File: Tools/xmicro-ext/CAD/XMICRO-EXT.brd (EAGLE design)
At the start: 101.6 x 101.6 mm, 2 parts

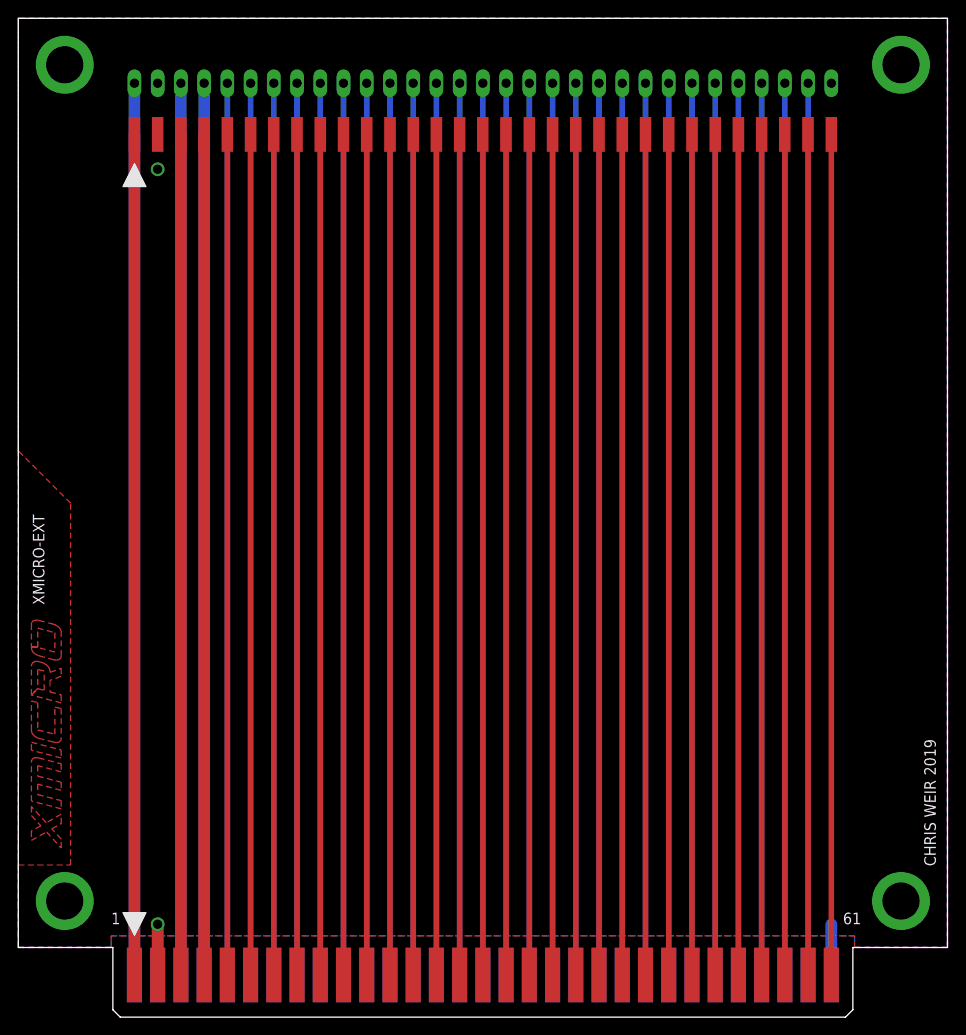
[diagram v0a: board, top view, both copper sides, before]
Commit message: XMICRO-EXT: Modified connector footprint
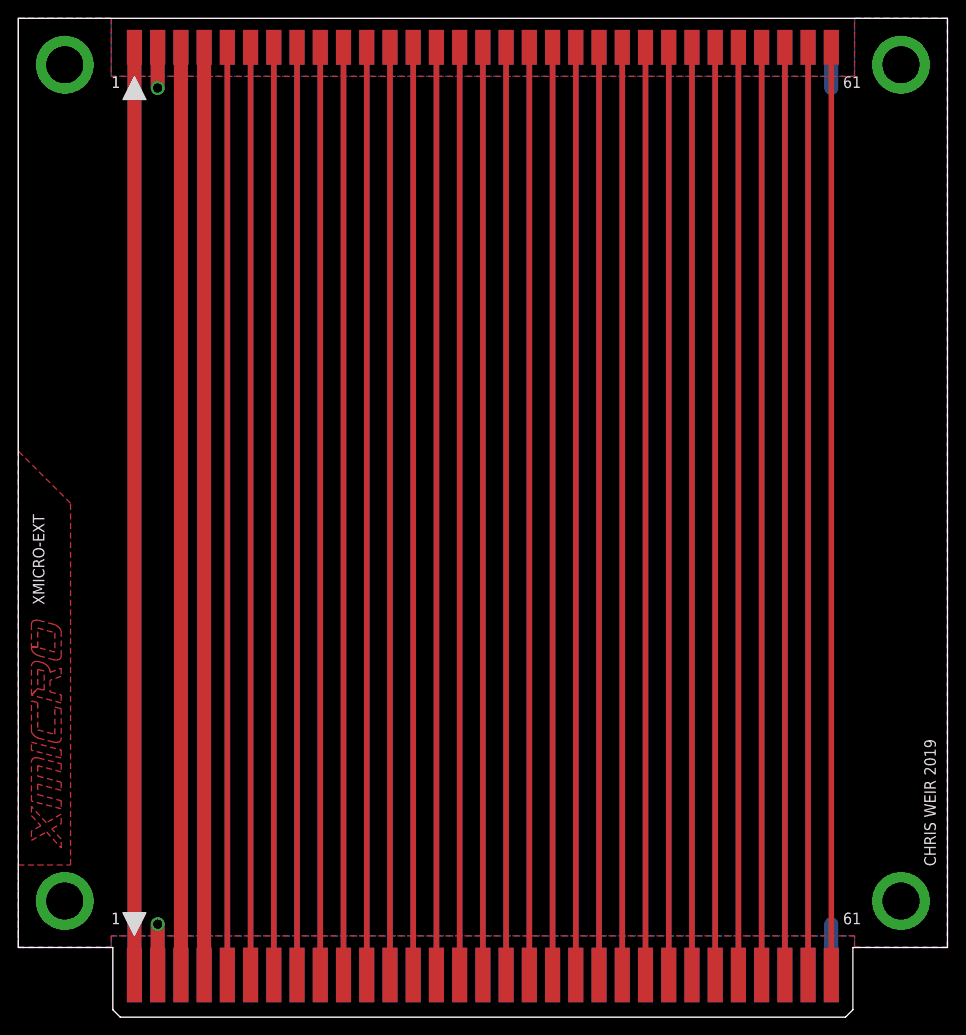
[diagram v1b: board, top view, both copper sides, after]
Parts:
- moved U$2 9.52 mm to (50.8, 101.6)
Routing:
- net GND: track 16.6 -> 30.0 mm
- net N$9: track 91.9 -> 101.4 mm
- net N$7: track 91.9 -> 101.4 mm
- net N$61: track 91.9 -> 101.4 mm
- net N$59: track 91.9 -> 101.4 mm
- net N$57: track 91.9 -> 101.4 mm
- net N$55: track 91.9 -> 101.4 mm
- net N$53: track 91.9 -> 101.4 mm
- net N$51: track 91.9 -> 101.4 mm
- net N$5: track 91.9 -> 101.4 mm
- net N$49: track 91.9 -> 101.4 mm
- net N$47: track 91.9 -> 101.4 mm
- net N$45: track 91.9 -> 101.4 mm
- net N$43: track 91.9 -> 101.4 mm
- net N$41: track 91.9 -> 101.4 mm
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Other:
- board text added: "V1 1943"
- board text removed: "V1 1912"
